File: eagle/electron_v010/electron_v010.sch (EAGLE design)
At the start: 92 parts, among them J1 SIM-NANO-4FF, J2 IPEX-20279-001E, U1 U-BLOX-SARA-U260, U2 SN74AVC4T245, U3 STM32F205RG, U4 MAX1704X, U5 SN74LVC1G07, U6 SN74LVC1G07, U8 SN74AVC4T245, X1 USB-MICROB, Y1 32Khz, Y2 26Mhz

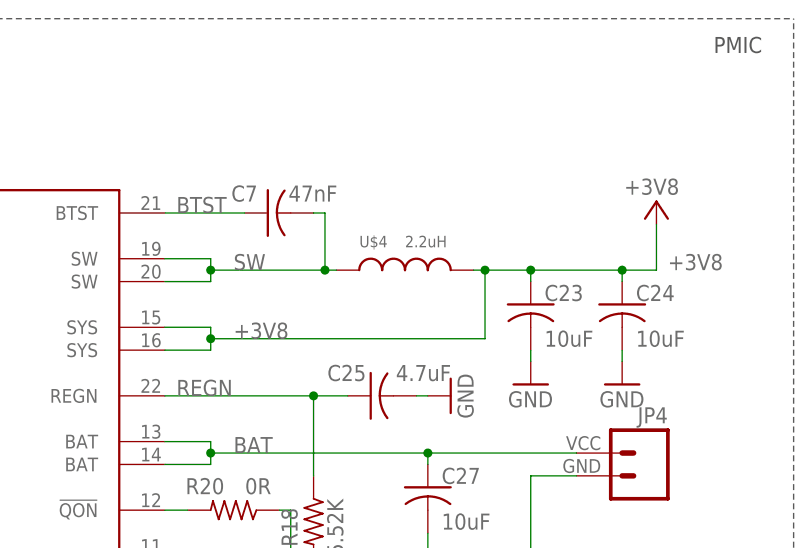
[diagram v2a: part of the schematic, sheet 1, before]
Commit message: #12 Updated to bigger pads PMIC inductor footprint and power polygons
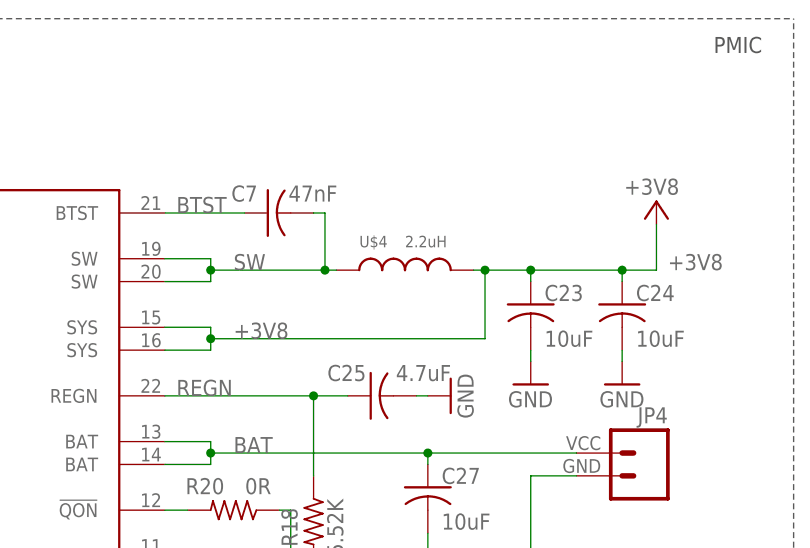
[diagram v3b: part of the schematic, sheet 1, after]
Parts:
- U$4: device electron:INDUCTOR4020 -> Particle:INDUCTORH
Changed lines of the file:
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@@
 <part name="U$3" library="Spark" deviceset="DIODE" device=""/>
 <part name="GND47" library="supply1" deviceset="GND" device=""/>
-<part name="U$4" library="electron" deviceset="INDUCTOR" device="4020" value="2.2uH"/>
+<part name="U$4" library="Particle" deviceset="INDUCTOR" device="H" value="2.2uH"/>
 <part name="+3V3" library="supply1" deviceset="+3V3" device=""/>
 <part name="+3V7" library="supply1" deviceset="+3V3" device="" value="+3V8"/>
@@
 <instance part="U$3" gate="G$1" x="113.03" y="167.64"/>
 <instance part="GND47" gate="1" x="193.04" y="105.41"/>
-<instance part="U$4" gate="L$1" x="203.2" y="154.94" smashed="yes">
+<instance part="U$4" gate="G$1" x="203.2" y="154.94" smashed="yes" rot="R90">
 <attribute name="NAME" x="198.12" y="157.48" size="1.27" layer="95"/>
 <attribute name="VALUE" x="203.2" y="157.48" size="1.27" layer="96"/>
@@
 <label x="232.41" y="154.94" size="1.778" layer="95"/>
 <label x="184.15" y="147.32" size="1.778" layer="95"/>
-<pinref part="U$4" gate="L$1" pin="2"/>
+<pinref part="U$4" gate="G$1" pin="2"/>
 <pinref part="C23" gate="G$1" pin="1"/>
 <pinref part="C24" gate="G$1" pin="1"/>
@@
 <junction x="194.31" y="154.94"/>
 <label x="184.15" y="154.94" size="1.778" layer="95"/>
-<pinref part="U$4" gate="L$1" pin="1"/>
+<pinref part="U$4" gate="G$1" pin="1"/>
 <pinref part="C7" gate="G$1" pin="2"/>
 </segment>

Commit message: Updated 5V header pad to round with drill size same as other headers
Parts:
- JP3: device pinhead:PINHD-1X1 -> Particle:PINHD-1X1
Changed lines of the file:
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@@
 <part name="U$7" library="Particle" deviceset="M02_0.05_HEADER" device=""/>
 <part name="C39" library="Spark" deviceset="C-US" device="" value="1uF"/>
-<part name="JP3" library="pinhead" deviceset="PINHD-1X1" device=""/>
+<part name="JP3" library="Particle" deviceset="PINHD-1X1" device=""/>
 <part name="JP2" library="Particle" deviceset="M18" device="DPAD"/>
 </parts>
